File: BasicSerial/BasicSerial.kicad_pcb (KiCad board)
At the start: 2 copper layers, 99.9 x 73 mm, 15 parts, among them CN1 DB9_Male, J1 COM_SELECT, J2 IRQ_SELECT, J3 Bus_ISA_8bit, U1 16550, U2 74LS688 or GAL16V8, U3 GD75232N, U4 1.8432 MHz

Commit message: First pass at PCB layout complete.
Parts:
- CN1: value DB9_Male -> DB9 Male
- U1: value 16550 -> 16550/16C550
- U2: value 74LS688 or GAL16V8 -> 74LS688, 74HCT688 or GAL16V8
- moved U4 41.9 mm to (123.2, 77.5)
- moved C4 41.9 mm to (136.5, 74.9)
- moved C3 27.3 mm to (182.2, 74.9)
- moved U3 27.3 mm to (170.8, 74.9)
- moved C5 20.1 mm to (170.8, 104.1)
- moved C6 18.2 mm to (170.8, 113.7)
- moved C7 17.1 mm to (170.8, 123.2), turned to 270 degrees
- moved U2 7.01 mm to (104.8, 74.9)
- moved C1 6.99 mm to (160.7, 74.9)
- moved C2 6.98 mm to (116.2, 74.9)
- moved U1 6.98 mm to (141.6, 74.9)
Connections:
- U4 pad 4: GND -> VCC
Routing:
- net GND: track 24.5 -> 347.2 mm, vias 4 -> 47
- net VCC: track 697.0 -> 621.1 mm, vias 17 -> 1
- net Net-(U1-Pad36): track 61.7 -> 27.4 mm
- net /SER_PIN9: track 0.00 -> 34.0 mm
- net /SER_PIN3: track 49.7 -> 18.1 mm, vias 2 -> 0
- net Net-(U1-Pad37): track 54.2 -> 23.2 mm, vias 1 -> 0
- net UART_XIN: track 60.9 -> 31.1 mm
- net Net-(U1-Pad33): track 50.8 -> 22.6 mm, vias 1 -> 0
- net /SER_PIN4: track 0.00 -> 26.7 mm, vias 0 -> 2
- net +12V: track 69.8 -> 96.3 mm, vias 1 -> 2
- net -12V: track 40.4 -> 64.2 mm, vias 1 -> 0
- net /SER_PIN8: track 0.00 -> 22.7 mm
- net /SER_PIN7: track 49.5 -> 27.7 mm, vias 2 -> 0
- net /SER_PIN2: track 43.4 -> 24.5 mm
- net D3: track 88.4 -> 70.5 mm
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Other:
- net class Serial: clearance 0.46 -> 0.34
- board text added: "BASIC SERIAL"
- board text added: "COM1:"
- board text added: "COM2:"
- board text added: "COM3:"
- board text added: "COM4:"
- board text added: "IRQ SELECTION"
- board text added: "IRQ2"
- board text added: "IRQ3"
- board text added: "IRQ4"
- board text added: "IRQ5"
- board text added: "IRQ7"
- board text added: "PORT SELECTION"
- board text added: "SUGGESTED: COM1=IRQ4 COM2=IRQ3 COM3=IRQ4 COM4=IRQ3"
- board text added: "Version 1,0 Copyright (C) 2021 Titanium Studios Pty Ltd Creative Commons Attribution-ShareAlike 4.0 International"

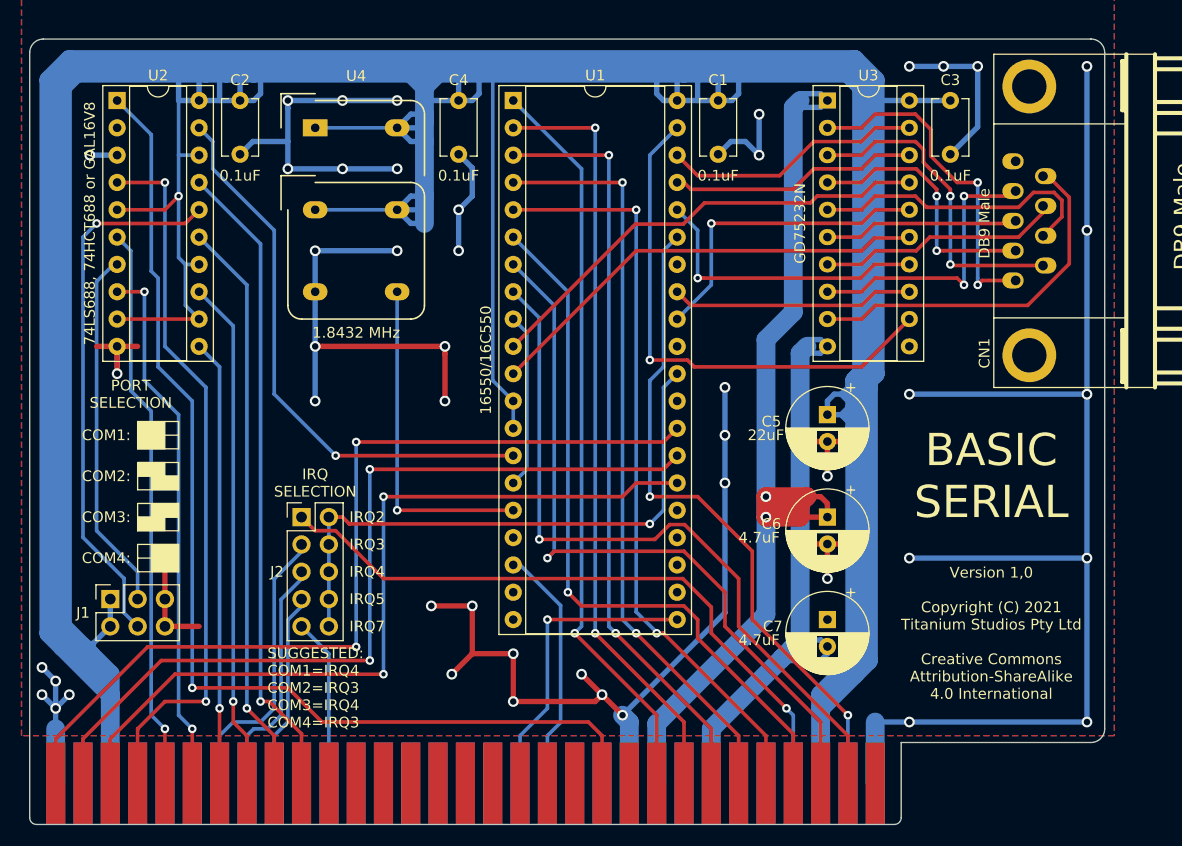
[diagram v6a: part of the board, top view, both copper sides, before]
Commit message: BasicSerial: Reduce 0.34mm track widths to 0.3mm. Minor sikscreen changes.
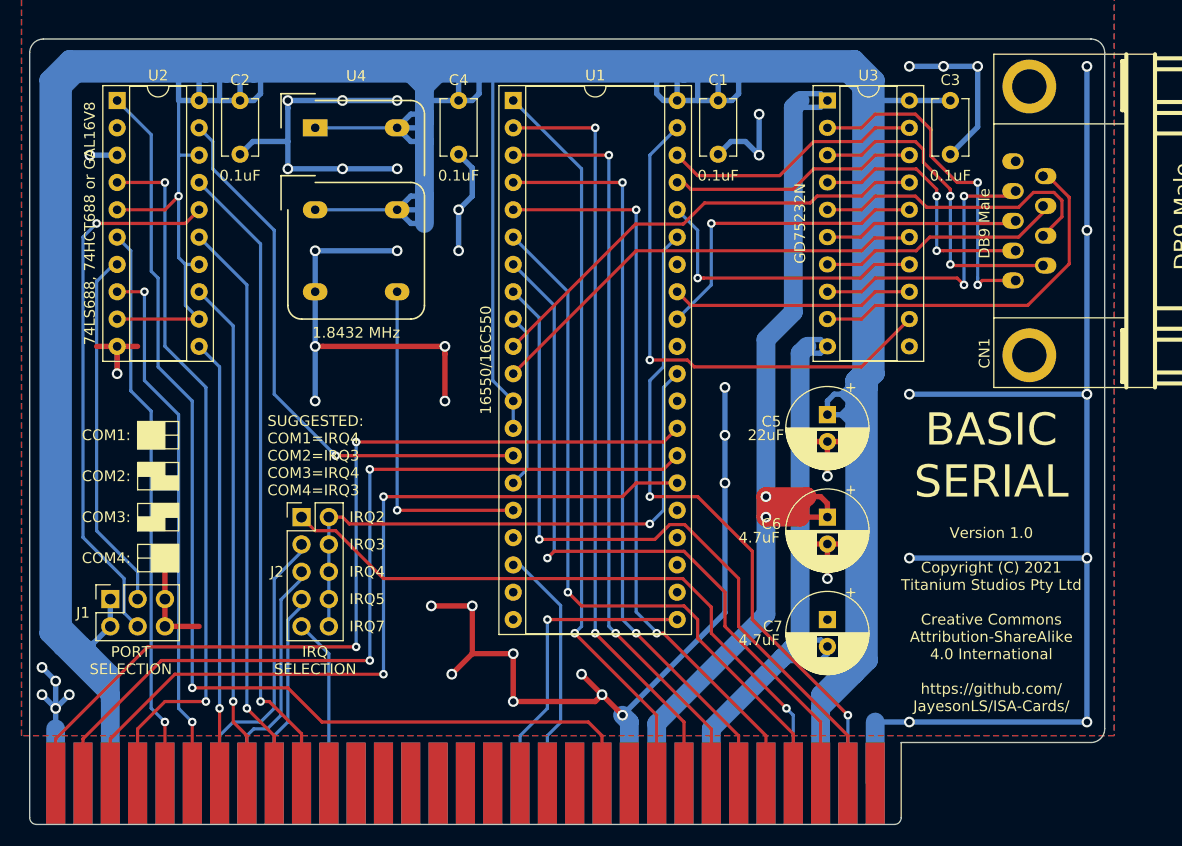
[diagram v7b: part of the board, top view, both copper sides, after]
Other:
- net class Default: clearance 0.24 -> 0.26; trace_width 0.34 -> 0.3
- net class Power: clearance 0.24 -> 0.26
- net class Serial: clearance 0.34 -> 0.36; trace_width 0.34 -> 0.3
- rule trace_clearance: 0.24 -> 0.26
- board text added: "Version 1.0 Copyright (C) 2021 Titanium Studios Pty Ltd Creative Commons Attribution-ShareAlike 4.0 International https://github.com/ JayesonLS/ISA-Cards/"
- board text removed: "Version 1,0 Copyright (C) 2021 Titanium Studios Pty Ltd Creative Commons Attribution-ShareAlike 4.0 International"
